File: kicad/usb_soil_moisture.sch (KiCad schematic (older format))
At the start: 2 parts, among them U1 SeeeduinoXIAO, U2 SENO0193

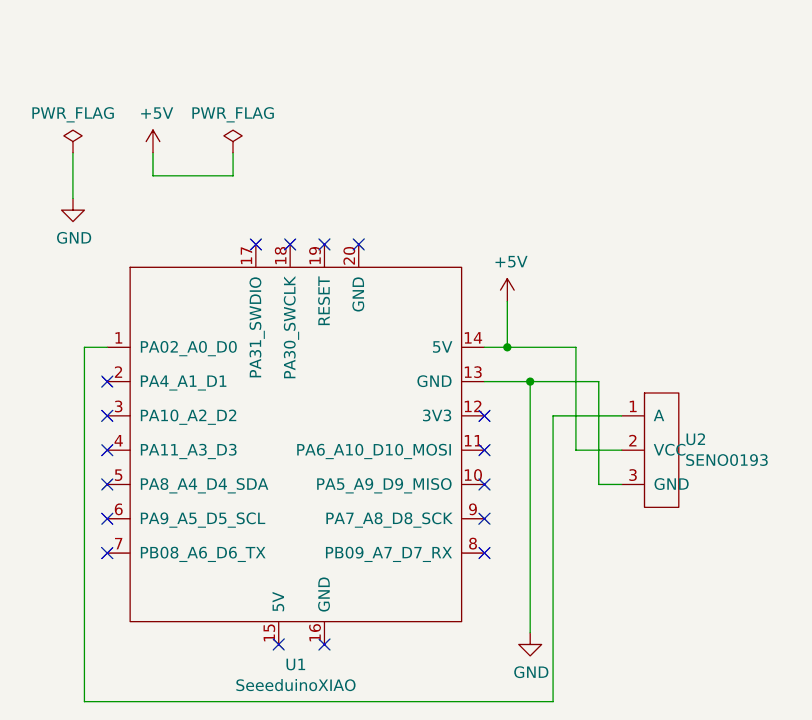
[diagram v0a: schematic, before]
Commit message: SENO0193のパッドが紐付かない現象を修正
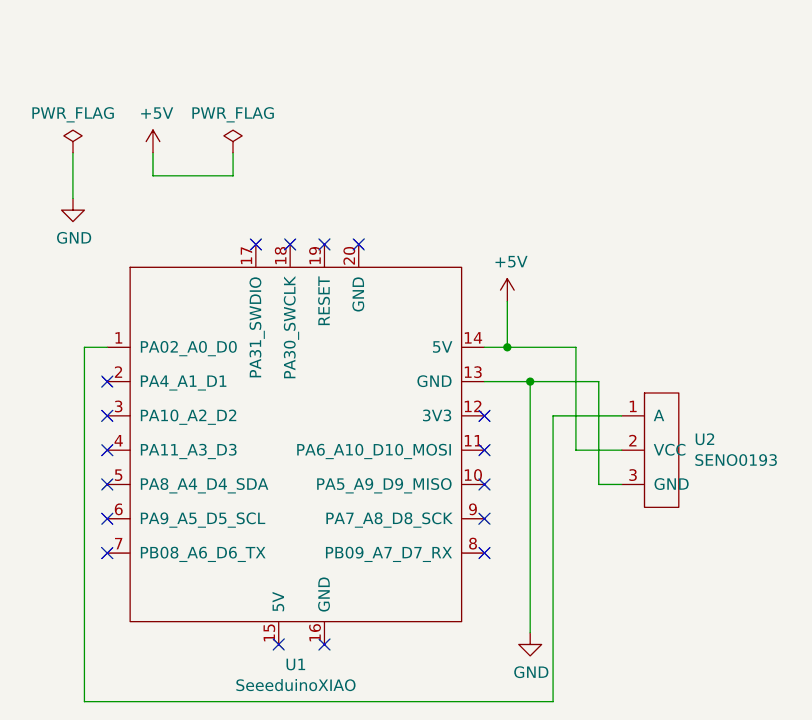
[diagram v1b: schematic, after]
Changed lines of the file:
@@
-$EndComp
-$Comp
-L kicad_mylib:SENO0193 U2
-U 1 1 6079E8C8
-P 3350 2400
-F 0 "U2" H 3528 2696 50  0000 L CNN
-F 1 "SENO0193" H 3528 2605 50  0000 L CNN
-F 2 "kicad_mylib:SENO0193" H 3400 2950 50  0001 C CNN
-F 3 "" H 3400 2950 50  0001 C CNN
-	1    3350 2400
-	1    0    0    -1
 $EndComp
 $Comp
@@
 	3150 1850 2850 1850
 Connection ~ 2850 1850
+$Comp
+L kicad_mylib:SENO0193 U2
+U 1 1 607A9A61
+P 3350 2400
+F 0 "U2" H 3568 2696 50  0000 L CNN
+F 1 "SENO0193" H 3568 2605 50  0000 L CNN
+F 2 "kicad_mylib:SENO0193" H 3400 2950 50  0001 C CNN
+F 3 "" H 3400 2950 50  0001 C CNN
+	1    3350 2400
+	1    0    0    -1
+$EndComp
 $EndSCHEMATC

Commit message: センサの電源を3.3Vに変更
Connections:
- net labels added: +3V3
- net labels removed: +5V
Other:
- moved on the sheet: U2
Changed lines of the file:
@@
 $EndComp
+$Comp
+L power:GND #PWR01
+U 1 1 6079C164
+P 850 1050
+F 0 "#PWR01" H 850 800 50  0001 C CNN
+F 1 "GND" H 855 877 50  0000 C CNN
+F 2 "" H 850 1050 50  0001 C CNN
+F 3 "" H 850 1050 50  0001 C CNN
+	1    850  1050
+	1    0    0    -1
+$EndComp
+Wire Wire Line
+	850  850  850  1050
+Wire Wire Line
+	1200 850  1200 950
+$Comp
+L power:GND #PWR04
+U 1 1 607A0BDB
+P 2850 2950
+F 0 "#PWR04" H 2850 2700 50  0001 C CNN
+F 1 "GND" H 2855 2777 50  0000 C CNN
+F 2 "" H 2850 2950 50  0001 C CNN
+F 3 "" H 2850 2950 50  0001 C CNN
+	1    2850 2950
+	1    0    0    -1
+$EndComp
+Wire Wire Line
+	2650 1850 2850 1850
+Wire Wire Line
+	2850 1850 2850 2950
+Wire Wire Line
+	1000 1700 900  1700
+Wire Wire Line
+	900  1700 900  3250
+NoConn ~ 1000 1850
+NoConn ~ 1000 2000
+NoConn ~ 1000 2150
+NoConn ~ 1000 2300
+NoConn ~ 1000 2450
+NoConn ~ 1000 2600
+NoConn ~ 1750 3000
+NoConn ~ 1950 3000
+NoConn ~ 2650 2600
+NoConn ~ 2650 2450
+NoConn ~ 2650 2300
+NoConn ~ 2650 2150
+$Comp
+L kicad_mylib:SENO0193 U2
+U 1 1 607A9A61
+P 3350 2700
+F 0 "U2" H 3568 2996 50  0000 L CNN
+F 1 "SENO0193" H 3568 2905 50  0000 L CNN
+F 2 "kicad_mylib:SENO0193" H 3400 3250 50  0001 C CNN
+F 3 "" H 3400 3250 50  0001 C CNN
+	1    3350 2700
+	1    0    0    -1
+$EndComp
+NoConn ~ 2100 1250
+NoConn ~ 1950 1250
+NoConn ~ 1800 1250
+NoConn ~ 1650 1250
+$Comp
+L Seeeduino_XIAO:SeeeduinoXIAO U1
+U 1 1 6079D694
+P 1850 2150
+F 0 "U1" H 1825 1211 50  0000 C CNN
+F 1 "SeeeduinoXIAO" H 1825 1120 50  0000 C CNN
+F 2 "kicad_mylib:SeeedXIAO" H 1500 2350 50  0001 C CNN
+F 3 "" H 1500 2350 50  0001 C CNN
+	1    1850 2150
+	1    0    0    -1
+$EndComp
+Wire Wire Line
+	1550 950  1550 850
+Wire Wire Line
+	1200 950  1550 950
 $Comp
 L power:PWR_FLAG #FLG02
@@
 $EndComp
 $Comp
-L power:GND #PWR01
-U 1 1 6079C164
-P 850 1050
-F 0 "#PWR01" H 850 800 50  0001 C CNN
-F 1 "GND" H 855 877 50  0000 C CNN
-F 2 "" H 850 1050 50  0001 C CNN
-F 3 "" H 850 1050 50  0001 C CNN
-	1    850  1050
-	1    0    0    -1
-$EndComp
-$Comp
-L power:+5V #PWR02
-U 1 1 6079C280
+L power:+3V3 #PWR0101
+U 1 1 60898A70
 P 1200 850
-F 0 "#PWR02" H 1200 700 50  0001 C CNN
-F 1 "+5V" H 1215 1023 50  0000 C CNN
+F 0 "#PWR0101" H 1200 700 50  0001 C CNN
+F 1 "+3V3" H 1215 1023 50  0000 C CNN
 F 2 "" H 1200 850 50  0001 C CNN
 F 3 "" H 1200 850 50  0001 C CNN
@@
 	1    0    0    -1
 $EndComp
-Wire Wire Line
-	850  850  850  1050
-Wire Wire Line
-	1200 850  1200 950
-Wire Wire Line
-	1200 950  1550 950
-Wire Wire Line
-	1550 950  1550 850
 $Comp
-L Seeeduino_XIAO:SeeeduinoXIAO U1
-U 1 1 6079D694
-P 1850 2150
-F 0 "U1" H 1825 1211 50  0000 C CNN
-F 1 "SeeeduinoXIAO" H 1825 1120 50  0000 C CNN
-F 2 "kicad_mylib:SeeedXIAO" H 1500 2350 50  0001 C CNN
-F 3 "" H 1500 2350 50  0001 C CNN
-	1    1850 2150
-	1    0    0    -1
-$EndComp
-$Comp
-L power:+5V #PWR03
-U 1 1 6079F78D
-P 2750 1500
-F 0 "#PWR03" H 2750 1350 50  0001 C CNN
-F 1 "+5V" H 2765 1673 50  0000 C CNN
-F 2 "" H 2750 1500 50  0001 C CNN
-F 3 "" H 2750 1500 50  0001 C CNN
-	1    2750 1500
-	1    0    0    -1
-$EndComp
-$Comp
-L power:GND #PWR04
-U 1 1 607A0BDB
-P 2850 2950
-F 0 "#PWR04" H 2850 2700 50  0001 C CNN
-F 1 "GND" H 2855 2777 50  0000 C CNN
-F 2 "" H 2850 2950 50  0001 C CNN
-F 3 "" H 2850 2950 50  0001 C CNN
-	1    2850 2950
+L power:+3V3 #PWR0102
+U 1 1 6089904F
+P 2750 1600
+F 0 "#PWR0102" H 2750 1450 50  0001 C CNN
+F 1 "+3V3" H 2765 1773 50  0000 C CNN
+F 2 "" H 2750 1600 50  0001 C CNN
+F 3 "" H 2750 1600 50  0001 C CNN
+	1    2750 1600
 	1    0    0    -1
 $EndComp
 Wire Wire Line
-	2750 1500 2750 1700
+	2750 1600 2750 2000
 Wire Wire Line
-	2750 1700 2650 1700
+	2750 2000 2650 2000
 Wire Wire Line
-	2650 1850 2850 1850
+	2750 2000 2950 2000
 Wire Wire Line
-	2850 1850 2850 2950
+	2950 2000 2950 2450
 Wire Wire Line
-	1000 1700 900  1700
+	2950 2450 3250 2450
+Connection ~ 2750 2000
 Wire Wire Line
-	900  1700 900  3250
+	3250 2600 3050 2600
 Wire Wire Line
-	900  3250 2950 3250
+	3050 2600 3050 1850
 Wire Wire Line
-	2950 3250 2950 2000
-NoConn ~ 1650 1250
-NoConn ~ 1800 1250
-NoConn ~ 1950 1250
-NoConn ~ 2100 1250
-NoConn ~ 1000 1850
-NoConn ~ 1000 2000
-NoConn ~ 1000 2150
-NoConn ~ 1000 2300
-NoConn ~ 1000 2450
-NoConn ~ 1000 2600
-NoConn ~ 1750 3000
-NoConn ~ 1950 3000
-NoConn ~ 2650 2600
-NoConn ~ 2650 2450
-NoConn ~ 2650 2300
-NoConn ~ 2650 2150
-NoConn ~ 2650 2000
-Wire Wire Line
-	2950 2000 3250 2000
-Wire Wire Line
-	3250 2150 3050 2150
-Wire Wire Line
-	3050 2150 3050 1700
-Wire Wire Line
-	3050 1700 2750 1700
-Connection ~ 2750 1700
+	3050 1850 2850 1850
+Connection ~ 2850 1850
 Wire Wire Line
 	3250 2300 3150 2300
 Wire Wire Line
-	3150 2300 3150 1850
+	3150 2300 3150 3250
 Wire Wire Line
-	3150 1850 2850 1850
-Connection ~ 2850 1850
-$Comp
-L kicad_mylib:SENO0193 U2
-U 1 1 607A9A61
-P 3350 2400
-F 0 "U2" H 3568 2696 50  0000 L CNN
-F 1 "SENO0193" H 3568 2605 50  0000 L CNN
-F 2 "kicad_mylib:SENO0193" H 3400 2950 50  0001 C CNN
-F 3 "" H 3400 2950 50  0001 C CNN
-	1    3350 2400
-	1    0    0    -1
-$EndComp
+	900  3250 3150 3250
+NoConn ~ 2650 1700
 $EndSCHEMATC
